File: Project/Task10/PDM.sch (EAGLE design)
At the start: 49 parts

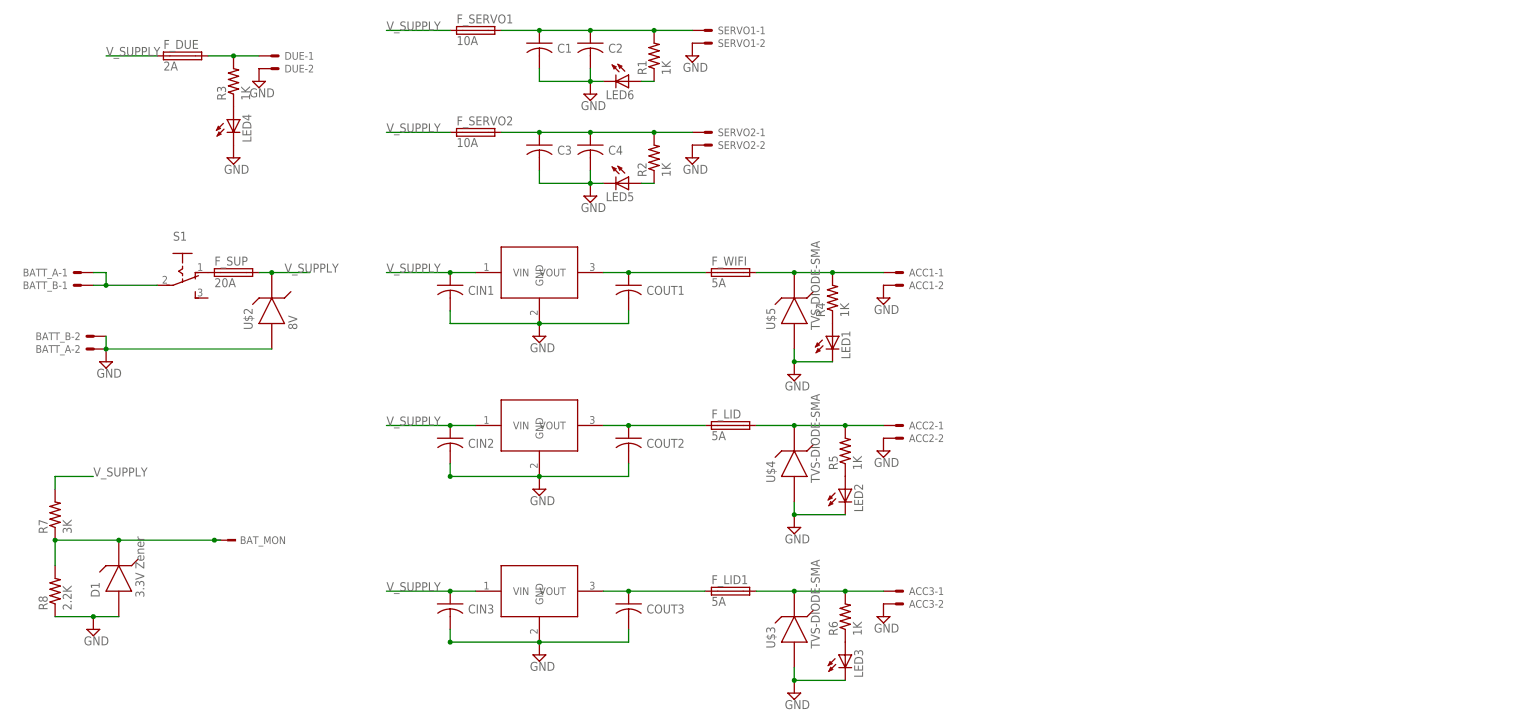
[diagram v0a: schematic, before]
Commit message: Task 10- Chose R, C, LED pkg, started BOM
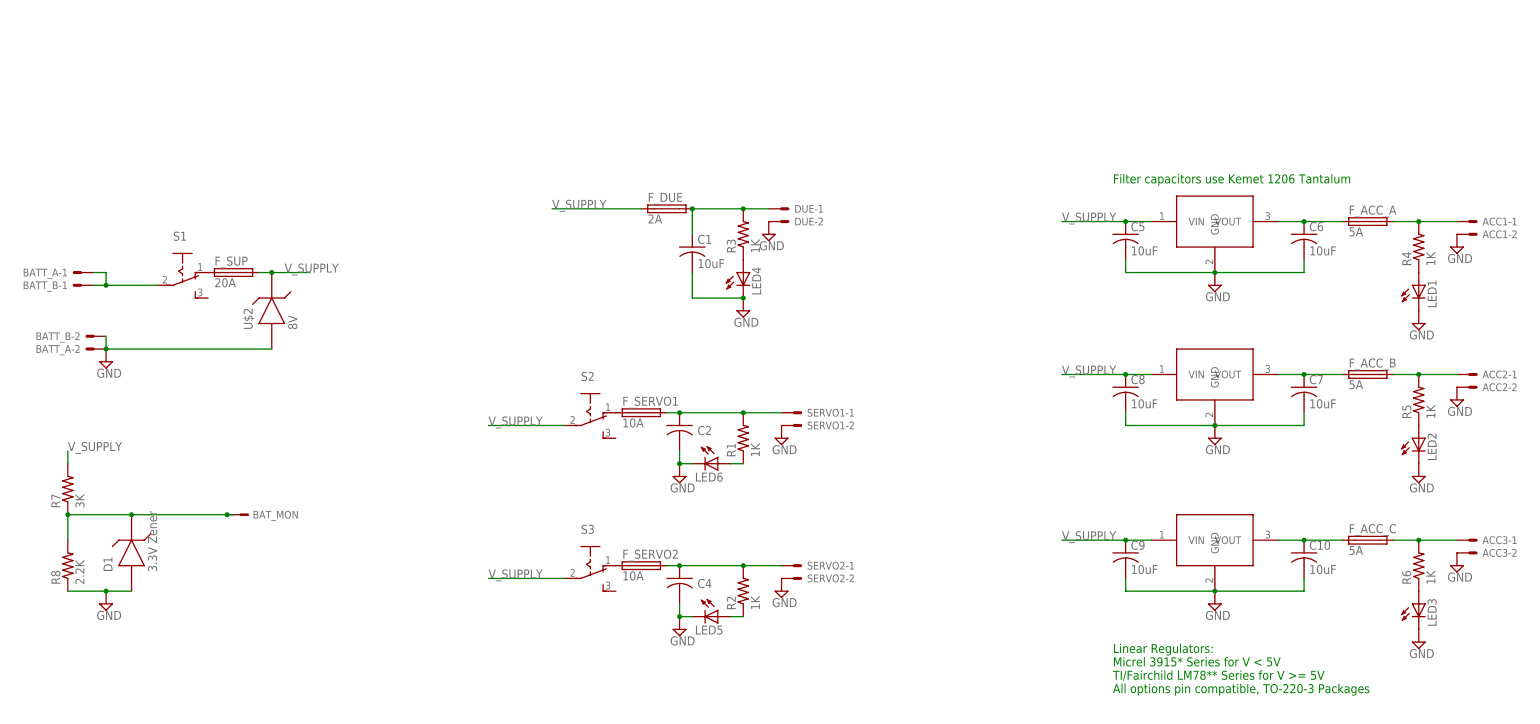
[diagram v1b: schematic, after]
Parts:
- removed C3, CIN1, CIN2, CIN3, COUT1, COUT2, COUT3: CAPACITORTH_CAP, TinyGadget(1):CAPACITORTH_CAP
- removed F_LID, F_LID1, F_WIFI: 5A, fuse:GSH15
- removed U$3, U$4, U$5: TVS-DIODE-SMA, Task5:TVS-DIODE-SMA
- added C10, C5, C6, C7, C8, C9: 10uF, rcl:C-USC1206K
- added F_ACC_A, F_ACC_B, F_ACC_C: 5A, fuse:GSH15
- added S2, S3: (no value), switch:255SB
- C1: value CAPACITORTH_CAP -> 10uF; device TinyGadget(1):CAPACITORTH_CAP -> rcl:C-USC1206K
- LED1, LED2, LED3, LED4, LED5, LED6: device led:LEDCHIP-LED0805 -> led:LEDSML1206
- R1, R2, R3, R4, R5, R6, R7, R8: device rcl:R-US_0309/10 -> rcl:R-US_R1206
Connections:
- new net N$12: F_SERVO2.1, S3.O
- new net N$3: F_SERVO1.1, S2.O
- net GND: now also C10.2, C5.2, C6.2, C7.2, C8.2, C9.2; no longer C3.2, CIN1.2, CIN2.2, CIN3.2, COUT1.2, COUT2.2, COUT3.2, U$3.AN, U$4.AN, U$5.AN
- net N$1: no longer C3.1
- net N$15: no longer C1.1
- net N$19: now also C10.1, F_ACC_C.1; no longer COUT3.1, F_LID1.1
- net N$2: now also F_ACC_B.2; no longer F_LID.2, U$4.CAT
- net N$21: now also F_ACC_C.2; no longer F_LID1.2, U$3.CAT
- net N$4: now also C1.1
- net N$6: now also C6.1, F_ACC_A.1; no longer COUT1.1, F_WIFI.1
- net N$7: now also F_ACC_A.2; no longer F_WIFI.2, U$5.CAT
- net N$9: now also C7.1, F_ACC_B.1; no longer COUT2.1, F_LID.1
- net V_SUPPLY: now also C5.1, C8.1, C9.1, S2.P, S3.P; no longer CIN1.1, CIN2.1, CIN3.1, F_SERVO1.1, F_SERVO2.1
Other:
- note added: "Filter capacitors use Kemet 1206 Tantalum"
- note added: "Linear Regulators: Micrel 3915* Series for V < 5V TI/Fairchild LM78** Series for V >= 5V All options pin compatible, TO-220-3 Packages"
- moved on the sheet: ACC1-1, ACC1-2, ACC2-1, ACC2-2, ACC3-1, ACC3-2, BAT_MON, C1, C2, C4, D1, DUE-1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

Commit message: Fixed diode packages and symbols
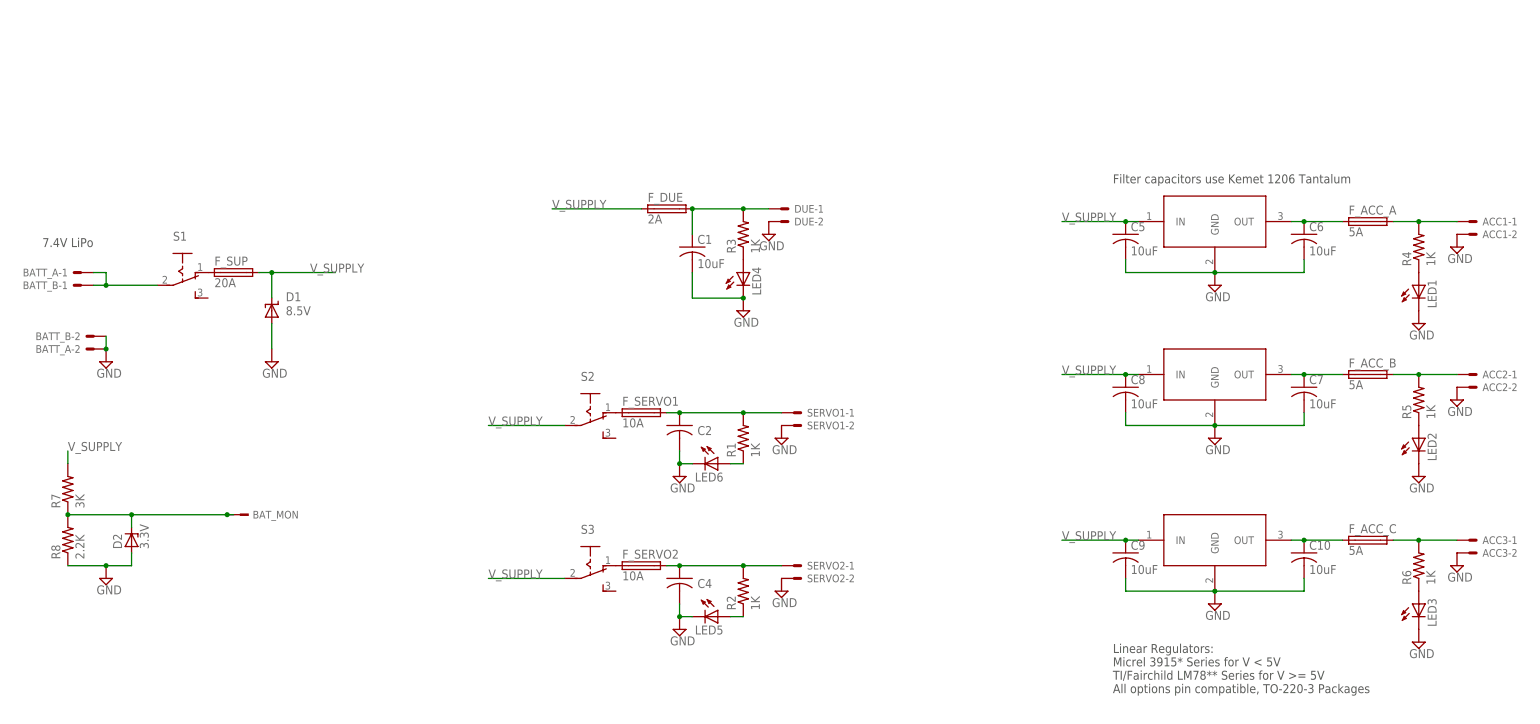
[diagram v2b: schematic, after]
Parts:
- removed U$2: 8V, Task5:TVS-DIODE-SMA
- removed U$6, U$7: MIC29150/29300/29500, Task5:MIC29150/29300/29500
- added D2: 3.3V, diode:ZENER-DIODESMB
- added U$3, U$4: MIC29150/29300/29500, MRSDTeamB:MIC29150/29300/29500
- D1: value 3.3V Zener -> 8.5V; device Task5:TVS-DIODE-SMA -> MRSDTeamB:SUPPRESSOR-SMBJ
- U$1: device Task5:MIC29150/29300/29500 -> MRSDTeamB:MIC29150/29300/29500
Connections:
- net GND: now also D1.A, D2.A, U$3.GND, U$4.GND; no longer D1.AN, U$2.AN, U$6.GND, U$7.GND
- net N$18: now also D2.C; no longer D1.CAT
- net N$19: now also U$4.OUT; no longer U$1.VOUT
- net N$6: now also U$1.OUT; no longer U$7.VOUT
- net N$9: now also U$3.OUT; no longer U$6.VOUT
- net V_SUPPLY: now also D1.C, U$1.IN, U$3.IN, U$4.IN; no longer U$1.VIN, U$2.CAT, U$6.VIN, U$7.VIN
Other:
- note added: "7.4V LiPo"
- moved on the sheet: R8

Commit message: Added PDR and Sketchup Resources
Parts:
- removed BATT_A, BATT_B: 22-23-2021, con-molex:22-23-2021
- removed F_ACC_A, F_ACC_B, F_ACC_C: 5A, fuse:GSH15
- added BATT1, BATT2: 5566-2, con-molex:5566-2
- DUE: value C-GRID-02-70553 -> 5566-2; device con-molex:C-GRID-02-70553 -> con-molex:5566-2
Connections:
- net GND: now also BATT1-2.S, BATT2-2.S; no longer BATT_A-2.S, BATT_B-2.S
- net N$10: now also BATT1-1.S, BATT2-1.S; no longer BATT_A-1.S, BATT_B-1.S
- net N$19: no longer F_ACC_C.1
- net N$2: no longer F_ACC_B.2
- net N$21: no longer F_ACC_C.2
- net N$6: no longer F_ACC_A.1
- net N$7: no longer F_ACC_A.2
- net N$9: no longer F_ACC_B.1
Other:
- moved on the sheet: ACC1-1, ACC1-2, ACC2-1, ACC2-2, ACC3-1, ACC3-2, C1, DUE-1, DUE-2, F_DUE, LED1, LED2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

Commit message: Changed TO-220 Package to Horizontal
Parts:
- removed U$4: MIC29150/29300/29500, MRSDTeamB:MIC29150/29300/29500
- added U$2: MIC29150/29300/29500HORIZONTAL, MRSDTeamB:MIC29150/29300/29500HORIZONTAL
- U$1, U$3: value MIC29150/29300/29500 -> MIC29150/29300/29500HORIZONTAL; device MRSDTeamB:MIC29150/29300/29500 -> MRSDTeamB:MIC29150/29300/29500HORIZONTAL
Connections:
- net GND: now also U$2.GND; no longer U$4.GND
- net N$19: now also U$3.OUT; no longer U$4.OUT
- net N$9: now also U$2.OUT; no longer U$3.OUT
- net V_SUPPLY: now also U$2.IN; no longer U$4.IN
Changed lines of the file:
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@@
 <part name="S2" library="switch" deviceset="255SB" device=""/>
 <part name="S3" library="switch" deviceset="255SB" device=""/>
-<part name="U$1" library="MRSDTeamB" deviceset="MIC29150/29300/29500" device=""/>
-<part name="U$3" library="MRSDTeamB" deviceset="MIC29150/29300/29500" device=""/>
-<part name="U$4" library="MRSDTeamB" deviceset="MIC29150/29300/29500" device=""/>
 <part name="SUPPLY10" library="supply2" deviceset="GND" device=""/>
 <part name="D1" library="MRSDTeamB" deviceset="SUPPRESSOR-" device="SMBJ" value="8.5V"/>
@@
 <part name="BATT1" library="con-molex" deviceset="5566-2" device="" value=""/>
 <part name="BATT2" library="con-molex" deviceset="5566-2" device="" value=""/>
+<part name="U$1" library="MRSDTeamB" deviceset="MIC29150/29300/29500" device="HORIZONTAL"/>
+<part name="U$2" library="MRSDTeamB" deviceset="MIC29150/29300/29500" device="HORIZONTAL"/>
+<part name="U$3" library="MRSDTeamB" deviceset="MIC29150/29300/29500" device="HORIZONTAL"/>
 </parts>
 <sheets>
@@
 <instance part="S2" gate="1" x="132.08" y="142.24" rot="R270"/>
 <instance part="S3" gate="1" x="132.08" y="111.76" rot="R270"/>
-<instance part="U$1" gate="G$1" x="256.54" y="177.8"/>
-<instance part="U$3" gate="G$1" x="256.54" y="147.32"/>
-<instance part="U$4" gate="G$1" x="256.54" y="114.3"/>
 <instance part="SUPPLY10" gate="GND" x="68.58" y="152.4"/>
 <instance part="D1" gate="G$1" x="68.58" y="162.56"/>
@@
 <instance part="BATT2" gate="-1" x="30.48" y="167.64" rot="MR0"/>
 <instance part="BATT2" gate="-2" x="30.48" y="154.94" rot="MR0"/>
+<instance part="U$1" gate="G$1" x="256.54" y="177.8"/>
+<instance part="U$2" gate="G$1" x="256.54" y="147.32"/>
+<instance part="U$3" gate="G$1" x="256.54" y="114.3"/>
 </instances>
 <busses>
@@
 <pinref part="C6" gate="G$1" pin="1"/>
 <wire x1="274.32" y1="180.34" x2="281.94" y2="180.34" width="0.1524" layer="91"/>
-<pinref part="U$1" gate="G$1" pin="OUT"/>
 <wire x1="274.32" y1="180.34" x2="271.78" y2="180.34" width="0.1524" layer="91"/>
 <junction x="274.32" y="180.34"/>
+<pinref part="U$1" gate="G$1" pin="OUT"/>
 </segment>
 </net>
@@
 <pinref part="C7" gate="G$1" pin="1"/>
 <wire x1="274.32" y1="149.86" x2="281.94" y2="149.86" width="0.1524" layer="91"/>
-<pinref part="U$3" gate="G$1" pin="OUT"/>
 <wire x1="274.32" y1="149.86" x2="271.78" y2="149.86" width="0.1524" layer="91"/>
 <junction x="274.32" y="149.86"/>
+<pinref part="U$2" gate="G$1" pin="OUT"/>
 </segment>
 </net>
@@
 <pinref part="C8" gate="G$1" pin="2"/>
 <wire x1="238.76" y1="139.7" x2="238.76" y2="142.24" width="0.1524" layer="91"/>
-<pinref part="U$3" gate="G$1" pin="GND"/>
+<pinref part="U$2" gate="G$1" pin="GND"/>
 </segment>
 <segment>
@@
 <pinref part="C9" gate="G$1" pin="2"/>
 <wire x1="238.76" y1="106.68" x2="238.76" y2="109.22" width="0.1524" layer="91"/>
-<pinref part="U$4" gate="G$1" pin="GND"/>
+<pinref part="U$3" gate="G$1" pin="GND"/>
 </segment>
 <segment>
@@
 <pinref part="C10" gate="G$1" pin="1"/>
 <wire x1="274.32" y1="116.84" x2="281.94" y2="116.84" width="0.1524" layer="91"/>
-<pinref part="U$4" gate="G$1" pin="OUT"/>
 <wire x1="274.32" y1="116.84" x2="271.78" y2="116.84" width="0.1524" layer="91"/>
 <junction x="274.32" y="116.84"/>
+<pinref part="U$3" gate="G$1" pin="OUT"/>
 </segment>
 </net>
@@
 <pinref part="C5" gate="G$1" pin="1"/>
 <wire x1="238.76" y1="180.34" x2="226.06" y2="180.34" width="0.1524" layer="91"/>
-<pinref part="U$1" gate="G$1" pin="IN"/>
 <wire x1="238.76" y1="180.34" x2="241.3" y2="180.34" width="0.1524" layer="91"/>
 <junction x="238.76" y="180.34"/>
+<pinref part="U$1" gate="G$1" pin="IN"/>
 </segment>
 <segment>
@@
 <label x="226.06" y="149.86" size="1.778" layer="95"/>
 <pinref part="C8" gate="G$1" pin="1"/>
-<pinref part="U$3" gate="G$1" pin="IN"/>
 <wire x1="238.76" y1="149.86" x2="241.3" y2="149.86" width="0.1524" layer="91"/>
 <junction x="238.76" y="149.86"/>
+<pinref part="U$2" gate="G$1" pin="IN"/>
 </segment>
 <segment>
@@
 <pinref part="C9" gate="G$1" pin="1"/>
 <wire x1="238.76" y1="116.84" x2="226.06" y2="116.84" width="0.1524" layer="91"/>
-<pinref part="U$4" gate="G$1" pin="IN"/>
 <wire x1="238.76" y1="116.84" x2="241.3" y2="116.84" width="0.1524" layer="91"/>
 <junction x="238.76" y="116.84"/>
-</segment>
-<segment>
+<pinref part="U$3" gate="G$1" pin="IN"/>
+</segment>
+<segment>

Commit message: Added ATO Fuseholders, Spec'd main switch
Moved main power switch/EStop to Batt harness (No PCB-Mount 20A switches
available).
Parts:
- removed F_SUP: 20A, fuse:GSH15
- removed S1: (no value), switch:255SB
- added F_BATT: 20A, MRSDTeamB:FUSE-ATO
- F_DUE, F_SERVO1, F_SERVO2: device fuse:GSH15 -> MRSDTeamB:FUSE-ATO
- renumbered S2 to SERVO1_PWR, S3 to SERVO2_PWR
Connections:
- removed net N$14 (its old number): F_SUP.1, S1.O
- net N$10: now also F_BATT.1; no longer S1.P
- net V_SUPPLY: now also F_BATT.2; no longer F_SUP.2

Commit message: ERC Errors Corrected
Several lines were not connected. Fixed.
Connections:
- removed net N$2: ACC2-1.S, R5.2
- removed net N$21: ACC3-1.S, R6.2
- removed net N$7: ACC1-1.S, R4.2
- net N$19: now also ACC3-1.S, R6.2
- net N$6: now also ACC1-1.S, R4.2
- net N$9: now also ACC2-1.S, R5.2
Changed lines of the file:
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@@
 <segment>
 <pinref part="C6" gate="G$1" pin="1"/>
-<wire x1="274.32" y1="180.34" x2="281.94" y2="180.34" width="0.1524" layer="91"/>
 <wire x1="274.32" y1="180.34" x2="271.78" y2="180.34" width="0.1524" layer="91"/>
-<junction x="274.32" y="180.34"/>
 <pinref part="U$1" gate="G$1" pin="OUT"/>
-</segment>
-</net>
-<net name="N$7" class="0">
-<segment>
 <pinref part="ACC1" gate="-1" pin="S"/>
-<wire x1="281.94" y1="180.34" x2="287.02" y2="180.34" width="0.1524" layer="91"/>
 <pinref part="R4" gate="G$1" pin="2"/>
 <wire x1="287.02" y1="180.34" x2="294.64" y2="180.34" width="0.1524" layer="91"/>
+<wire x1="274.32" y1="180.34" x2="287.02" y2="180.34" width="0.1524" layer="91"/>
+<junction x="274.32" y="180.34"/>
 <junction x="287.02" y="180.34"/>
 </segment>
@@
 <segment>
 <pinref part="C7" gate="G$1" pin="1"/>
-<wire x1="274.32" y1="149.86" x2="281.94" y2="149.86" width="0.1524" layer="91"/>
 <wire x1="274.32" y1="149.86" x2="271.78" y2="149.86" width="0.1524" layer="91"/>
+<pinref part="U$2" gate="G$1" pin="OUT"/>
+<wire x1="294.64" y1="149.86" x2="287.02" y2="149.86" width="0.1524" layer="91"/>
+<pinref part="ACC2" gate="-1" pin="S"/>
+<pinref part="R5" gate="G$1" pin="2"/>
+<wire x1="274.32" y1="149.86" x2="287.02" y2="149.86" width="0.1524" layer="91"/>
 <junction x="274.32" y="149.86"/>
-<pinref part="U$2" gate="G$1" pin="OUT"/>
+<junction x="287.02" y="149.86"/>
 </segment>
 </net>
@@
 <pinref part="SUPPLY5" gate="GND" pin="GND"/>
 <pinref part="SERVO2" gate="-2" pin="S"/>
-</segment>
-</net>
-<net name="N$2" class="0">
-<segment>
-<wire x1="294.64" y1="149.86" x2="287.02" y2="149.86" width="0.1524" layer="91"/>
-<pinref part="ACC2" gate="-1" pin="S"/>
-<wire x1="287.02" y1="149.86" x2="281.94" y2="149.86" width="0.1524" layer="91"/>
-<pinref part="R5" gate="G$1" pin="2"/>
-<junction x="287.02" y="149.86"/>
 </segment>
 </net>
@@
 <segment>
 <pinref part="C10" gate="G$1" pin="1"/>
-<wire x1="274.32" y1="116.84" x2="281.94" y2="116.84" width="0.1524" layer="91"/>
 <wire x1="274.32" y1="116.84" x2="271.78" y2="116.84" width="0.1524" layer="91"/>
-<junction x="274.32" y="116.84"/>
 <pinref part="U$3" gate="G$1" pin="OUT"/>
-</segment>
-</net>
-<net name="N$21" class="0">
-<segment>
 <wire x1="294.64" y1="116.84" x2="287.02" y2="116.84" width="0.1524" layer="91"/>
 <pinref part="ACC3" gate="-1" pin="S"/>
-<wire x1="287.02" y1="116.84" x2="281.94" y2="116.84" width="0.1524" layer="91"/>
 <pinref part="R6" gate="G$1" pin="2"/>
+<wire x1="274.32" y1="116.84" x2="287.02" y2="116.84" width="0.1524" layer="91"/>
+<junction x="274.32" y="116.84"/>
 <junction x="287.02" y="116.84"/>
 </segment>

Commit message: Datahseet for XT60 for battery connector added
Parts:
- ACC1: value C-GRID-02-70553 -> 5566-2; device con-molex:C-GRID-02-70553 -> con-molex:5566-2
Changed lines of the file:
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@@
 <part name="ACC2" library="con-molex" deviceset="5566-2" device="" value=""/>
 <part name="SUPPLY5" library="supply2" deviceset="GND" device=""/>
-<part name="ACC1" library="con-molex" deviceset="C-GRID-02" device="-70553"/>
 <part name="SUPPLY6" library="supply2" deviceset="GND" device=""/>
 <part name="SUPPLY7" library="supply2" deviceset="GND" device=""/>
@@
 <part name="F_SERVO1" library="MRSDTeamB" deviceset="FUSE-" device="ATO" value="10A"/>
 <part name="F_SERVO2" library="MRSDTeamB" deviceset="FUSE-" device="ATO" value="10A"/>
+<part name="ACC1" library="con-molex" deviceset="5566-2" device="" value=""/>
 </parts>
 <sheets>
@@
 <instance part="ACC2" gate="-2" x="297.18" y="147.32"/>
 <instance part="SUPPLY5" gate="GND" x="170.18" y="106.68"/>
-<instance part="ACC1" gate="-2" x="297.18" y="177.8"/>
-<instance part="ACC1" gate="-1" x="297.18" y="180.34" smashed="yes">
-<attribute name="NAME" x="299.72" y="179.578" size="1.524" layer="95"/>
-</instance>
 <instance part="SUPPLY6" gate="GND" x="170.18" y="167.64"/>
 <instance part="SUPPLY7" gate="GND" x="294.64" y="175.26"/>
@@
 <instance part="F_SERVO1" gate="G$1" x="142.24" y="142.24"/>
 <instance part="F_SERVO2" gate="G$1" x="142.24" y="111.76"/>
+<instance part="ACC1" gate="-1" x="297.18" y="180.34"/>
+<instance part="ACC1" gate="-2" x="297.18" y="177.8"/>
 </instances>
 <busses>
@@
 <wire x1="274.32" y1="180.34" x2="271.78" y2="180.34" width="0.1524" layer="91"/>
 <pinref part="U$1" gate="G$1" pin="OUT"/>
-<pinref part="ACC1" gate="-1" pin="S"/>
 <pinref part="R4" gate="G$1" pin="2"/>
 <wire x1="287.02" y1="180.34" x2="294.64" y2="180.34" width="0.1524" layer="91"/>
@@
 <junction x="274.32" y="180.34"/>
 <junction x="287.02" y="180.34"/>
+<pinref part="ACC1" gate="-1" pin="S"/>
 </segment>
 </net>
@@
 </segment>
 <segment>
-<pinref part="ACC1" gate="-2" pin="S"/>
-<pinref part="SUPPLY7" gate="GND" pin="GND"/>
-</segment>
-<segment>
 <pinref part="ACC2" gate="-2" pin="S"/>
 <pinref part="SUPPLY9" gate="GND" pin="GND"/>
@@
 <pinref part="SERVO2" gate="-2" pin="S"/>
 </segment>
-</net>
+<segment>
+<pinref part="SUPPLY7" gate="GND" pin="GND"/>
+<pinref part="ACC1" gate="-2" pin="S"/>
+</segment>
+</net>
